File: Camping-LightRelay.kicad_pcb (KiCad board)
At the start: 2 copper layers, 43 x 63 mm, 62 parts, among them CN1 U262-061N-4BVC11, CN3 B2B-XH-A, CN4 907-152A1022D10200, CN5 907-152A1022D10200, J1 J300, J2 J300, J3 J300, J4 J300, Q1 IRF7404, Q2 BC847, U1 LMV358ID

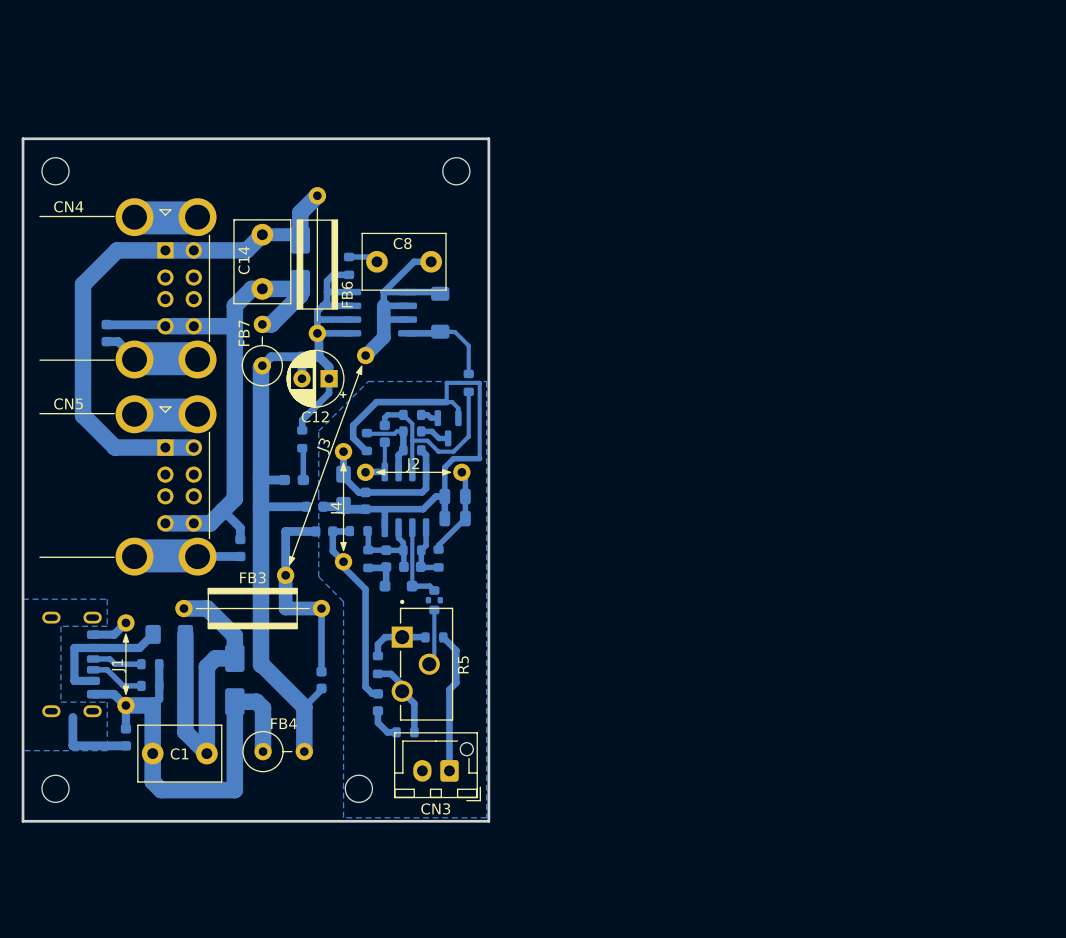
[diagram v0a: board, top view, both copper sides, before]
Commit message: Работа со схемой модуля
Частичная отрисовка и назначение посадочных мест субмодуля питания от PowerBank. *Работа продолжается*.
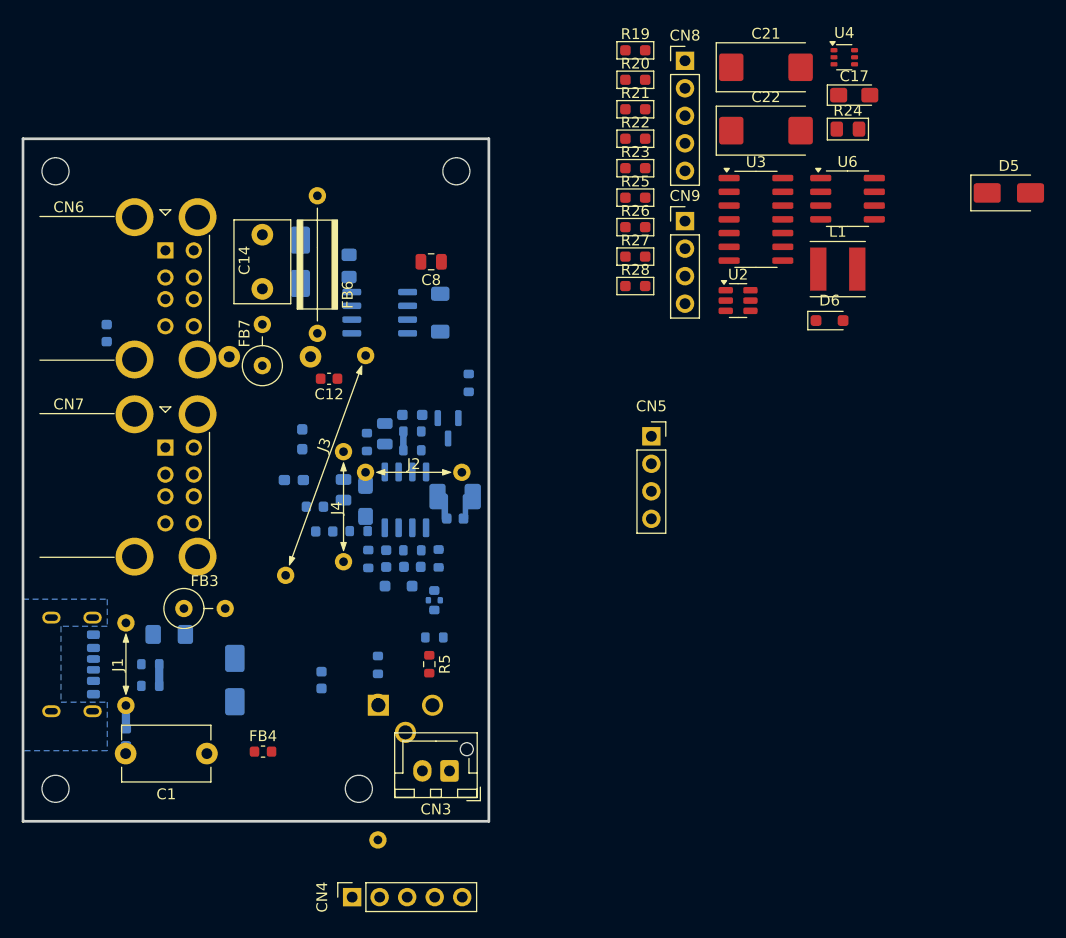
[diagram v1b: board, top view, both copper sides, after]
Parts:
- removed FB10: BLM18AG601SN1D, Inductor_SMD:L_0603_1608Metric
- added C17: 10uFx10V, Capacitor_Tantalum_SMD:CP_EIA-3216-12_Kemet-S_Pad1.58x1.35mm_HandSolder, F.Cu at (155.7, 39.0)
- added C21: 680uFx6.3V, Capacitor_Tantalum_SMD:CP_EIA-7343-43_Kemet-X_Pad2.25x2.55mm_HandSolder, F.Cu at (147.6, 36.4)
- added C22: 680uFx6.3V, Capacitor_Tantalum_SMD:CP_EIA-7343-43_Kemet-X_Pad2.25x2.55mm_HandSolder, F.Cu at (147.6, 42.2)
- added CN4: PM2.54-1*5, Connector_PinSocket_2.54mm:PinSocket_1x05_P2.54mm_Vertical, F.Cu at (109.4, 113.0)
- added CN5: PM2.54-1*4, Connector_PinSocket_2.54mm:PinSocket_1x04_P2.54mm_Vertical, F.Cu at (137.0, 70.5)
- added CN8: HB-PH3-25415PB2GOP, Connector_PinHeader_2.54mm:PinHeader_1x05_P2.54mm_Vertical, F.Cu at (140.1, 35.8)
- added CN9: HB-PH3-25414PB2GOP, Connector_PinHeader_2.54mm:PinHeader_1x04_P2.54mm_Vertical, F.Cu at (140.1, 50.6)
- added D5: SMAJ6.0A, Diode_SMD:D_SMA, F.Cu at (170.0, 48.0)
- added D6: SD05, Diode_SMD:D_SOD-323_HandSoldering, F.Cu at (153.4, 59.8)
- added L1: 47uH, Inductor_SMD:L_Taiyo-Yuden_NR-50xx, F.Cu at (154.2, 55.0)
- added R19: 2.7k, PCM_Resistor_SMD_AKL:R_0603_1608Metric_Pad0.98x0.95mm, F.Cu at (135.5, 34.8)
- added R20: 560, PCM_Resistor_SMD_AKL:R_0603_1608Metric_Pad0.98x0.95mm, F.Cu at (135.5, 37.6)
- added R21: 2.7k, PCM_Resistor_SMD_AKL:R_0603_1608Metric_Pad0.98x0.95mm, F.Cu at (135.5, 40.3)
- added R22: 10k, PCM_Resistor_SMD_AKL:R_0603_1608Metric_Pad0.98x0.95mm, F.Cu at (135.5, 43.0)
- added R23: 100k, PCM_Resistor_SMD_AKL:R_0603_1608Metric_Pad0.98x0.95mm, F.Cu at (135.5, 45.7)
- added R24: 10, PCM_Resistor_SMD_AKL:R_0805_2012Metric_Pad1.15x1.40mm, F.Cu at (155.1, 42.1)
- added R25: 2.7k, PCM_Resistor_SMD_AKL:R_0603_1608Metric_Pad0.98x0.95mm, F.Cu at (135.5, 48.4)
- added R26: 680k, PCM_Resistor_SMD_AKL:R_0603_1608Metric_Pad0.98x0.95mm, F.Cu at (135.5, 51.2)
- added R27: 22, PCM_Resistor_SMD_AKL:R_0603_1608Metric_Pad0.98x0.95mm, F.Cu at (135.5, 53.9)
- added R28: 1.2M, PCM_Resistor_SMD_AKL:R_0603_1608Metric_Pad0.98x0.95mm, F.Cu at (135.5, 56.6)
- added U2: USBLC6-2SC6, Package_TO_SOT_SMD:SOT-23-6, F.Cu at (145.0, 57.9)
- added U3: CD4011UBM, Package_SO:SOIC-14_3.9x8.7mm_P1.27mm, F.Cu at (146.7, 50.4)
- added U4: SI1865DDL, Package_TO_SOT_SMD:SOT-363_SC-70-6, F.Cu at (154.8, 35.5)
- added U6: TLC555DTR, Package_SO:SOIC-8_3.9x4.9mm_P1.27mm, F.Cu at (155.1, 48.5)
- C1: value 1500x2kV -> 2n2; footprint Capacitor_THT:C_Disc_D7.5mm_W5.0mm_P5.00mm -> Capacitor_THT:C_Disc_D8.0mm_W5.0mm_P7.50mm
- C10: value 10uF -> 56; footprint Capacitor_SMD:C_0805_2012Metric -> Capacitor_SMD:C_0603_1608Metric
- C11: value 0.1 -> 2n2; footprint Capacitor_SMD:C_0603_1608Metric -> Capacitor_THT:C_Disc_D8.0mm_W5.0mm_P7.50mm
- C12: value 100uFx10V -> 0.1; footprint Capacitor_THT:CP_Radial_D5.0mm_P2.50mm -> Capacitor_SMD:C_0603_1608Metric
- C13: value 56 -> 1uF; footprint Capacitor_SMD:C_0603_1608Metric -> Capacitor_SMD:C_0805_2012Metric
- C6: value 0.1 -> 10uFx10V; footprint Capacitor_SMD:C_0603_1608Metric -> Capacitor_Tantalum_SMD:CP_EIA-3216-10_Kemet-I_Pad1.58x1.35mm_HandSolder
- C7: value 10uFx10V -> 10uF; footprint Capacitor_Tantalum_SMD:CP_EIA-3216-10_Kemet-I_Pad1.58x1.35mm_HandSolder -> Capacitor_SMD:C_0805_2012Metric
- C8: value 1500x2kV -> 10uF; footprint Capacitor_THT:C_Disc_D7.5mm_W5.0mm_P5.00mm -> Capacitor_SMD:C_0805_2012Metric
- C9: value 10uF -> 100uFx10V; footprint Capacitor_SMD:C_0805_2012Metric -> Capacitor_Tantalum_SMD:CP_EIA-3528-15_AVX-H_Pad1.50x2.35mm_HandSolder
- D4: value SMAJ8.0A -> SMAJ6.0A
- FB2: value BLM18AG601SN1D -> XRRH3.5*8.0*0.8; footprint Inductor_SMD:L_0603_1608Metric -> PCM_Ferrite_THT_AKL:Ferrite_L8.0mm_D3.5mm_P12.70mm
- FB3: footprint PCM_Ferrite_THT_AKL:Ferrite_L8.0mm_D3.5mm_P12.70mm -> PCM_Ferrite_THT_AKL:Ferrite_L8.0mm_D3.5mm_P3.81mm_Vertical
- FB4: value XRRH3.5*8.0*0.8 -> BLM18AG601SN1D; footprint PCM_Ferrite_THT_AKL:Ferrite_L8.0mm_D3.5mm_P3.81mm_Vertical -> Inductor_SMD:L_0603_1608Metric
- R10: value 1.2M -> 2.2k
- R11: value 100k -> 120k
- R12: value 2.2k -> 560k
- R13: value 120k -> 10k
- R14: value 560k -> 10k
- R16, R17: value 10k -> 5.1k 1%; footprint Resistor_SMD:R_0603_1608Metric -> PCM_Resistor_SMD_AKL:R_0603_1608Metric_Pad0.98x0.95mm
- R18: value 1 -> 42; footprint Resistor_SMD:R_0603_1608Metric -> PCM_Resistor_SMD_AKL:R_0805_2012Metric_Pad1.15x1.40mm
- R3: value 5.1k 1% -> 180k 1%
- R4: value 180k 1% -> 200k; footprint Resistor_SMD:R_0603_1608Metric -> lib:TRIM_PTN10-A01HB20
- R5: value 200k -> 10k 1%; footprint lib:TRIM_PTN10-A01HB20 -> Resistor_SMD:R_0603_1608Metric
- R6: value 10k 1% -> 82k 1%
- R7: value 5.1k 1% -> 100k 1%
- R8: value 82k 1% -> 1.2M
- R9: value 100k 1% -> 100k
- renumbered CN4 to CN6, CN5 to CN7
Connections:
- C10 pad 1: Net-(J2-A) -> Net-(U1.2-+)
- C10 pad 2: GND -> Net-(CN5-Pin_3)
- C11 pad 1: Net-(C11-Pad1) -> Net-(CN6-VBUS1)
- C11 pad 2: GNDE -> Net-(CN6-GND1)
- C12 pad 1: Net-(C11-Pad1) -> /ScapPwrStorageModule/PBANK_VBUS
- C12 pad 2: GNDE -> GND2
- C13 pad 1: Net-(J2-B) -> Net-(D7-K)
- C13 pad 2: Net-(C13-Pad2) -> GND2
- C2 pad 1: Net-(R5-S) -> Net-(R4-S)
- C5 pad 1: +5V -> Net-(U1.1-V+)
- C5 pad 2: GNDE -> GND
- C6 pad 1: Net-(J4-A) -> Net-(U1.1-V+)
- C7 pad 1: Net-(J4-A) -> Net-(U1.2-+)
- C8 pad 1: Net-(D3-K) -> Net-(U1.2-+)
- C8 pad 2: Net-(C8-Pad2) -> GND
- C9 pad 1: Net-(J2-A) -> Net-(D4-A2)
- C9 pad 2: GND -> GNDE
- CN1 pad A12: Net-(J1-B) -> Net-(D1-A2)
- CN6 pad 1: Net-(CN4-VBUS1) -> Net-(CN6-VBUS1)
- CN6 pad 4: Net-(CN4-GND1) -> Net-(CN6-GND1)
- CN6 pad 5: Net-(CN4-VBUS1) -> Net-(CN6-VBUS1)
- CN6 pad 8: Net-(CN4-GND1) -> Net-(CN6-GND1)
- CN6 pad 9: Net-(CN4-Shield) -> Net-(CN6-Shield)
- CN7 pad 1: Net-(CN4-VBUS1) -> Net-(CN6-VBUS1)
- CN7 pad 4: Net-(CN4-GND1) -> Net-(CN6-GND1)
- CN7 pad 5: Net-(CN4-VBUS1) -> Net-(CN6-VBUS1)
- CN7 pad 8: Net-(CN4-GND1) -> Net-(CN6-GND1)
- CN7 pad 9: Net-(CN5-Shield) -> Net-(CN7-Shield)
- D3 pad 1: Net-(D3-K) -> Net-(CN4-Pin_1)
- D4 pad 1: Net-(CN4-VBUS1) -> Net-(CN4-Pin_1)
- D4 pad 2: Net-(CN4-GND1) -> Net-(D4-A2)
- FB2 pad 1: Net-(J4-B) -> Net-(D1-A1)
- FB2 pad 2: Net-(FB2-Pad2) -> Net-(CN4-Pin_1)
- FB3 pad 1: Net-(D1-A1) -> Net-(D1-A2)
- FB3 pad 2: +5V -> GNDE
- FB4 pad 1: Net-(D1-A2) -> Net-(CN5-Pin_4)
- FB4 pad 2: GNDE -> GND
- FB5 pad 2: Net-(J4-B) -> Net-(U1.1-V+)
- FB6 pad 1: Net-(C11-Pad1) -> Net-(D4-A2)
- FB6 pad 2: Net-(CN4-VBUS1) -> Net-(CN6-VBUS1)
- FB7 pad 2: Net-(CN4-GND1) -> Net-(CN6-GND1)
- FB8 pad 1: GNDE -> Net-(CN6-GND1)
- FB8 pad 2: GND -> Net-(CN6-Shield)
- FB9 pad 1: Net-(CN4-GND1) -> Net-(CN6-GND1)
- FB9 pad 2: Net-(CN4-Shield) -> Net-(CN7-Shield)
- Q1 pad 1: Net-(D3-K) -> Net-(CN4-Pin_1)
- Q1 pad 2: Net-(D3-K) -> Net-(CN4-Pin_1)
- Q1 pad 3: Net-(D3-K) -> Net-(CN4-Pin_1)
- Q1 pad 5: Net-(C11-Pad1) -> Net-(D4-A2)
- Q1 pad 6: Net-(C11-Pad1) -> Net-(D4-A2)
- Q1 pad 7: Net-(C11-Pad1) -> Net-(D4-A2)
- Q1 pad 8: Net-(C11-Pad1) -> Net-(D4-A2)
- R10 pad 1: Net-(U1.1-+) -> Net-(D3-A)
- R10 pad 2: Net-(C4-Pad2) -> Net-(CN5-Pin_3)
- R11 pad 1: Net-(C4-Pad2) -> Net-(U1.1-V+)
- R11 pad 2: Net-(J2-A) -> Net-(U1.2--)
- R12 pad 1: Net-(D3-A) -> Net-(U1.2--)
- R12 pad 2: Net-(C13-Pad2) -> GND
- R13 pad 1: Net-(J4-A) -> Net-(U1.2--)
- R13 pad 2: Net-(U1.2--) -> Net-(Q2-C)
- R14 pad 1: Net-(U1.2--) -> Net-(Q2-B)
- R14 pad 2: GND -> Net-(CN5-Pin_3)
- R15 pad 1: Net-(U1.2--) -> Net-(D4-A2)
- R15 pad 2: Net-(Q2-C) -> Net-(LED1-A)
- R16 pad 1: Net-(C11-Pad1) -> Net-(R16-Pad1)
- R16 pad 2: Net-(LED1-A) -> Net-(D6-A1)
- R17 pad 1: Net-(Q2-B) -> Net-(R17-Pad1)
- R17 pad 2: Net-(C13-Pad2) -> Net-(D6-A1)
- R18 pad 1: Net-(C8-Pad2) -> /ScapPwrStorageModule/PBANK_VBUS
- R18 pad 2: Net-(C11-Pad1) -> Net-(Q4-C)
- R2 pad 1: Net-(R5-E) -> Net-(R4-E)
- R2 pad 2: Net-(R5-A) -> Net-(R4-A)
- R3 pad 1: Net-(CN1-CC2) -> Net-(U1.1-V+)
- R3 pad 2: Net-(D1-A2) -> Net-(R4-E)
- R4 pad 1: Net-(FB2-Pad2) -> Net-(R4-A)
- R4 pad 2: Net-(R5-E) -> Net-(R4-S)
- R5 pad 1: Net-(R5-A) -> Net-(R4-A)
- R5 pad 2: Net-(R5-S) -> Net-(CN3-Pin_1)
- R6 pad 1: Net-(R5-A) -> Net-(U1.1-V+)
- R6 pad 2: Net-(CN3-Pin_1) -> Net-(U1.1-+)
- R7 pad 1: Net-(CN1-CC1) -> Net-(U1.1-+)
- R7 pad 2: Net-(D1-A2) -> GND
- R8 pad 1: Net-(J4-B) -> Net-(U1.1-+)
- R8 pad 2: Net-(U1.1-+) -> Net-(C4-Pad2)
- R9 pad 1: Net-(U1.1-+) -> Net-(C4-Pad2)
- R9 pad 2: GND -> Net-(U1.2-+)
- U1 pad 5: Net-(J2-B) -> Net-(U1.2-+)
- U1 pad 7: Net-(C13-Pad2) -> Net-(CN5-Pin_3)
- U1 pad 8: Net-(J4-A) -> Net-(U1.1-V+)
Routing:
- net Net-(CN4-GND1): track 53.1 -> 0.00 mm
- net GNDE: track 52.1 -> 0.00 mm
- net Net-(CN4-VBUS1): track 50.4 -> 0.00 mm
- net GND: track 51.9 -> 4.03 mm
- net Net-(D1-A2): track 42.1 -> 2.15 mm
- net Net-(D1-A1): track 30.5 -> 0.00 mm
- net Net-(C11-Pad1): track 29.2 -> 0.00 mm
- net Net-(D3-K): track 21.7 -> 0.00 mm
- net +5V: track 19.0 -> 0.00 mm
- net Net-(J4-B): track 18.6 -> 0.00 mm
- net Net-(C13-Pad2): track 18.5 -> 0.00 mm
- net Net-(CN5-Shield): track 15.5 -> 0.00 mm
- net Net-(CN4-Shield): track 15.4 -> 0.00 mm
- net Net-(J4-A): track 14.8 -> 0.00 mm
- net Net-(CN3-Pin_1): track 13.1 -> 0.00 mm
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- removed copper zone on B.Cu, net GND

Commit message: Переделка топологии субмодулей
Фотореле вынесен в отдельный субмодуль, как дополнительная печатная плата. Схема управления PowerBank-ом перенесена на силовую плату с другими компонентами.
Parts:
- moved CN8 27.9 mm to (127.0, 60.4)
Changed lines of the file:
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@@
 	(footprint "Connector_PinHeader_2.54mm:PinHeader_1x05_P2.54mm_Vertical"
 		(layer "F.Cu")
-		(at 140.105 35.8)
+		(at 127 60.38)
 		(descr "Through hole straight pin header, 1x05, 2.54mm pitch, single row")
 		(tags "Through hole pin header THT 1x05 2.54mm single row")
@@
 		)
 		(fp_text user "${REFERENCE}"
-			(at 0 5.08 360)
+			(at 0 5.08 0)
 			(layer "F.Fab")
 			(effects

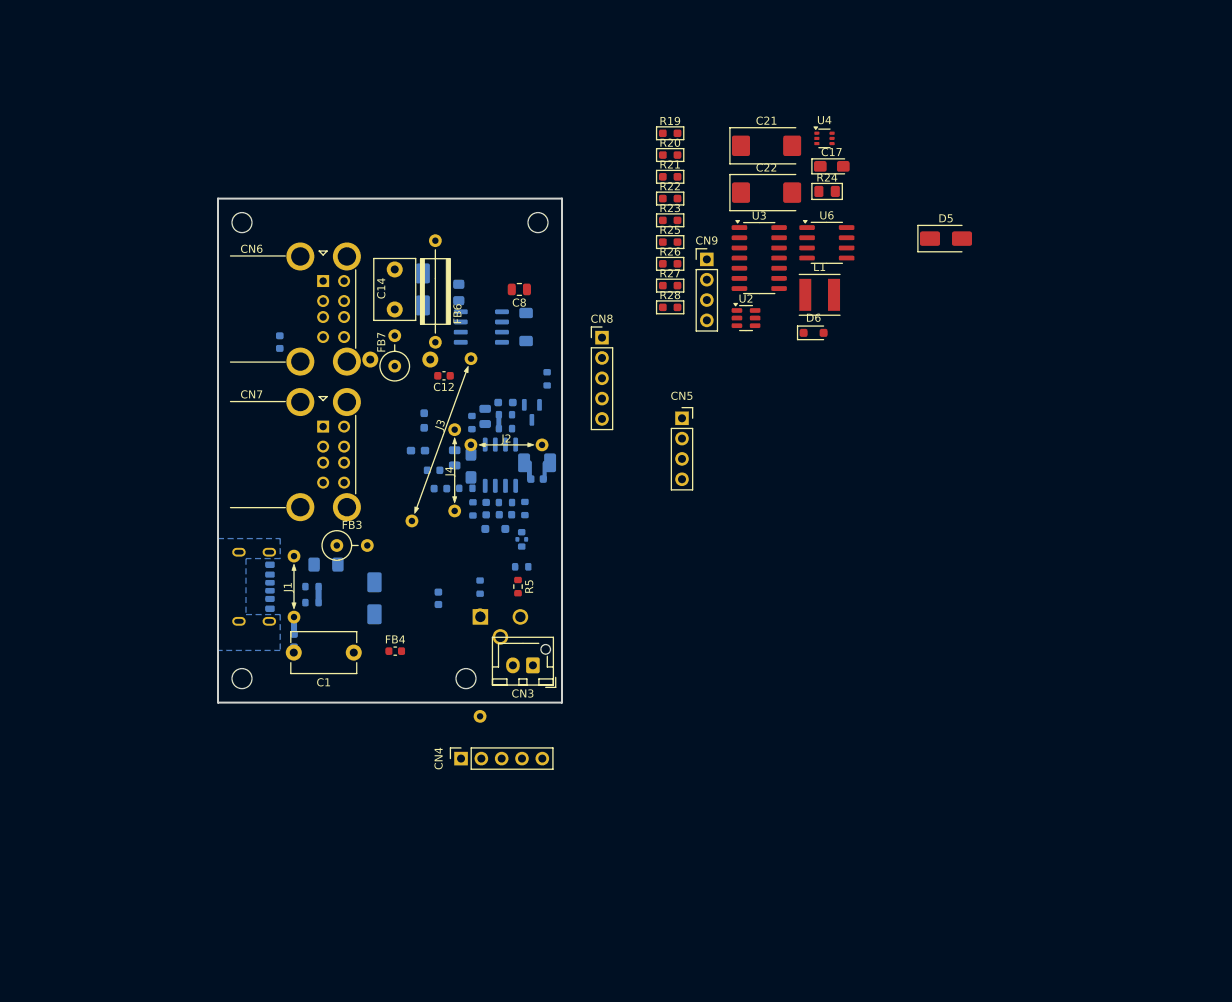
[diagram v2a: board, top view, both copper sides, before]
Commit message: Назначение посадочных мест схемы
Дорисовка недостающий э/компонентов и важных 3D-моделей
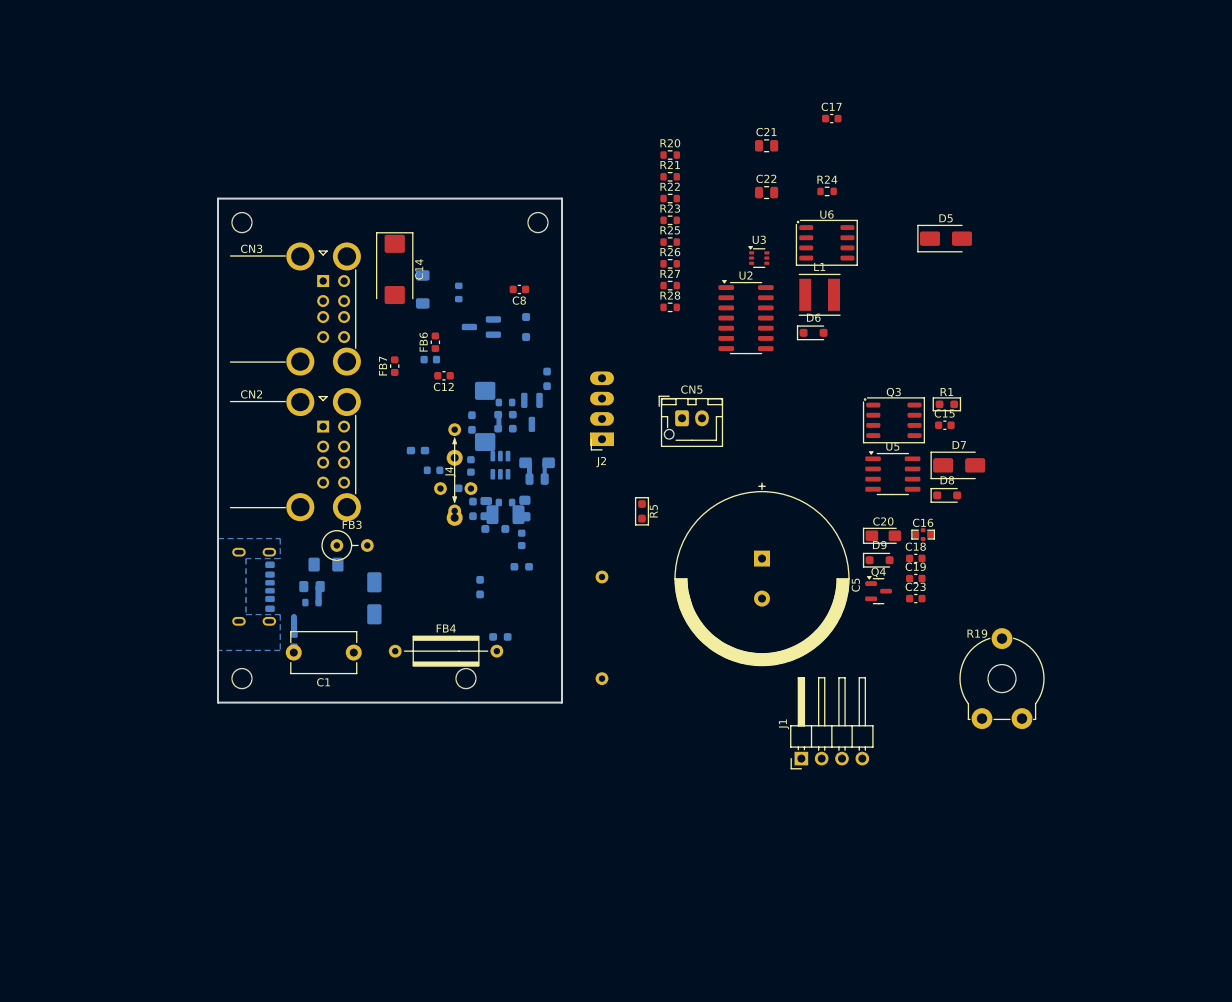
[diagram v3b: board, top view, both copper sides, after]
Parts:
- removed the CN3 at (118.4, 101.3)
- removed CN4: PM2.54-1*5, Connector_PinSocket_2.54mm:PinSocket_1x05_P2.54mm_Vertical
- removed CN8: HB-PH3-25415PB2GOP, Connector_PinHeader_2.54mm:PinHeader_1x05_P2.54mm_Vertical
- removed CN9: HB-PH3-25414PB2GOP, Connector_PinHeader_2.54mm:PinHeader_1x04_P2.54mm_Vertical
- removed FB9: BLM18AG601SN1D, Inductor_SMD:L_0603_1608Metric
- removed J3: J300, lib:Junction_850mil
- removed R16: 5.1k 1%, PCM_Resistor_SMD_AKL:R_0603_1608Metric_Pad0.98x0.95mm
- removed U4: SI1865DDL, Package_TO_SOT_SMD:SOT-363_SC-70-6
- added C15: 0.1, Capacitor_SMD:C_0603_1608Metric, F.Cu at (169.9, 71.3)
- added C16: 0.1, lib:C_0603_3-terminal, F.Cu at (167.1, 85.0)
- added C18: 56, Capacitor_SMD:C_0603_1608Metric, F.Cu at (166.2, 88.0)
- added C19: 0.1, Capacitor_SMD:C_0603_1608Metric, F.Cu at (166.2, 90.5)
- added C20: 10uFx10V, Capacitor_Tantalum_SMD:CP_EIA-3216-10_Kemet-I_Pad1.58x1.35mm_HandSolder, F.Cu at (162.2, 85.2)
- added C23: 56, Capacitor_SMD:C_0603_1608Metric, F.Cu at (166.2, 93.0)
- added D7: SMAJ6.0A, Diode_SMD:D_SMA, F.Cu at (171.7, 76.3)
- added D8: BAT20J, Diode_SMD:D_SOD-323_HandSoldering, F.Cu at (170.2, 80.1)
- added D9: SD05, Diode_SMD:D_SOD-323_HandSoldering, F.Cu at (161.7, 88.2)
- added Q3: IRF7404, PCM_Package_SO_AKL:SO-8_3.9x4.9mm_P1.27mm, F.Cu at (163.5, 70.7)
- added Q4: BC847, Package_TO_SOT_SMD:SOT-23, F.Cu at (161.6, 92.1)
- added R1: 5.1k 1%, PCM_Resistor_SMD_AKL:R_0603_1608Metric_Pad0.98x0.95mm, F.Cu at (170.1, 68.7)
- added U5: TLC555DTR, Package_SO:SOIC-8_3.9x4.9mm_P1.27mm, F.Cu at (163.4, 77.4)
- C10: value 56 -> 1uF; footprint Capacitor_SMD:C_0603_1608Metric -> Capacitor_SMD:C_0805_2012Metric
- C11: value 2n2 -> 0.1; footprint Capacitor_THT:C_Disc_D8.0mm_W5.0mm_P7.50mm -> Capacitor_SMD:C_0603_1608Metric
- C13: value 1uF -> 680uFx6.3V; footprint Capacitor_SMD:C_0805_2012Metric -> Capacitor_Tantalum_SMD:CP_EIA-7343-43_Kemet-X_Pad2.25x2.55mm_HandSolder
- C14: value 1500x2kV -> 680uFx6.3V; footprint Capacitor_THT:C_Disc_D7.5mm_W5.0mm_P5.00mm -> Capacitor_Tantalum_SMD:CP_EIA-7343-43_Kemet-X_Pad2.25x2.55mm_HandSolder
- C17: value 10uFx10V -> 0.1; footprint Capacitor_Tantalum_SMD:CP_EIA-3216-12_Kemet-S_Pad1.58x1.35mm_HandSolder -> Capacitor_SMD:C_0603_1608Metric
- C2: footprint lib:C_0603_3-terminal -> Capacitor_SMD:C_0603_1608Metric
- C21, C22: value 680uFx6.3V -> 10uF; footprint Capacitor_Tantalum_SMD:CP_EIA-7343-43_Kemet-X_Pad2.25x2.55mm_HandSolder -> Capacitor_SMD:C_0805_2012Metric
- C3: value 0.1 -> 1uF; footprint Capacitor_SMD:C_0603_1608Metric -> Capacitor_SMD:C_0805_2012Metric
- C4: value 56 -> 100uFx10V; footprint Capacitor_SMD:C_0603_1608Metric -> Capacitor_Tantalum_SMD:CP_EIA-3528-15_AVX-H_Pad1.50x2.35mm_HandSolder
- C5: value 0.1 -> 1.5Fx5.5V; footprint Capacitor_SMD:C_0603_1608Metric -> lib:Eaton_KR-5R5C155; moved to F.Cu
- C6: value 10uFx10V -> 10n; footprint Capacitor_Tantalum_SMD:CP_EIA-3216-10_Kemet-I_Pad1.58x1.35mm_HandSolder -> Capacitor_SMD:C_0603_1608Metric
- C7: value 10uF -> 2n2; footprint Capacitor_SMD:C_0805_2012Metric -> Capacitor_THT:C_Disc_D8.0mm_W5.0mm_P7.50mm
- C8: value 10uF -> 10n; footprint Capacitor_SMD:C_0805_2012Metric -> Capacitor_SMD:C_0603_1608Metric
- C9: value 100uFx10V -> 10uFx10V; footprint Capacitor_Tantalum_SMD:CP_EIA-3528-15_AVX-H_Pad1.50x2.35mm_HandSolder -> Capacitor_Tantalum_SMD:CP_EIA-3216-12_Kemet-S_Pad1.58x1.35mm_HandSolder
- CN5: value PM2.54-1*4 -> B2B-XH-A; footprint Connector_PinSocket_2.54mm:PinSocket_1x04_P2.54mm_Vertical -> Connector_JST:JST_XH_B2B-XH-AM_1x02_P2.50mm_Vertical
- D3: value BZV55C6V8 -> BAT20J; footprint Diode_SMD:D_MiniMELF -> Diode_SMD:D_SOD-323_HandSoldering
- D4: value SMAJ6.0A -> BZV55C6V8; footprint Diode_SMD:D_SMA -> Diode_SMD:D_MiniMELF
- D6: value SD05 -> BAT20J
- FB4: value BLM18AG601SN1D -> XRRH3.5*8.0*0.8; footprint Inductor_SMD:L_0603_1608Metric -> PCM_Ferrite_THT_AKL:Ferrite_L8.0mm_D3.5mm_P12.70mm
- FB5: value BLM18AG601SN1D -> XRRH3.5*8.0*0.8; footprint Inductor_SMD:L_0603_1608Metric -> PCM_Ferrite_THT_AKL:Ferrite_L8.0mm_D3.5mm_P3.81mm_Vertical
- FB6: value XRRH3.5*8.0*0.8 -> BLM18AG601SN1D; footprint PCM_Ferrite_THT_AKL:Ferrite_L8.0mm_D3.5mm_P12.70mm -> Inductor_SMD:L_0603_1608Metric
- FB7: value XRRH3.5*8.0*0.8 -> BLM18AG601SN1D; footprint PCM_Ferrite_THT_AKL:Ferrite_L8.0mm_D3.5mm_P3.81mm_Vertical -> Inductor_SMD:L_0603_1608Metric
- J1: value J300 -> PH2.54-07-04PWD; footprint lib:Junction_300mil -> Connector_PinHeader_2.54mm:PinHeader_1x04_P2.54mm_Horizontal
- J2: value J300 -> ~; footprint lib:Junction_350mil -> lib:PinSolder_1x04_P2.54mm
- Q1: value IRF7404 -> FDV301N; footprint PCM_Package_SO_AKL:SO-8_3.9x4.9mm_P1.27mm -> PCM_Package_TO_SOT_SMD_AKL:SOT-23_BigPads
- Q2: value BC847 -> BC817; footprint Package_TO_SOT_SMD:SOT-23 -> PCM_Package_TO_SOT_SMD_AKL:SOT-23_BigPads
- R10: value 2.2k -> 10k
- R11: value 120k -> 10; footprint Resistor_SMD:R_0603_1608Metric -> PCM_Resistor_SMD_AKL:R_0805_2012Metric_Pad1.15x1.40mm
- R12: value 560k -> 2.7k; footprint Resistor_SMD:R_0603_1608Metric -> PCM_Resistor_SMD_AKL:R_0603_1608Metric_Pad0.98x0.95mm
- R13: value 10k -> 680k; footprint Resistor_SMD:R_0603_1608Metric -> PCM_Resistor_SMD_AKL:R_0603_1608Metric_Pad0.98x0.95mm
- R14: value 10k -> 22; footprint Resistor_SMD:R_0603_1608Metric -> PCM_Resistor_SMD_AKL:R_0603_1608Metric_Pad0.98x0.95mm
- R15: value 10k -> 1.2M; footprint Resistor_SMD:R_0603_1608Metric -> PCM_Resistor_SMD_AKL:R_0603_1608Metric_Pad0.98x0.95mm
- R17: value 5.1k 1% -> 1.8M; footprint PCM_Resistor_SMD_AKL:R_0603_1608Metric_Pad0.98x0.95mm -> Resistor_SMD:R_0603_1608Metric
- R18: value 42 -> 180k 1%; footprint PCM_Resistor_SMD_AKL:R_0805_2012Metric_Pad1.15x1.40mm -> Resistor_SMD:R_0603_1608Metric
- R19: value 2.7k -> 200k; footprint PCM_Resistor_SMD_AKL:R_0603_1608Metric_Pad0.98x0.95mm -> lib:Potentiometer_Bochen_PT10
- R2: value 1.8M -> 5.1k 1%; footprint Resistor_SMD:R_0603_1608Metric -> PCM_Resistor_SMD_AKL:R_0603_1608Metric_Pad0.98x0.95mm
- R20: value 560 -> 10k 1%; footprint PCM_Resistor_SMD_AKL:R_0603_1608Metric_Pad0.98x0.95mm -> Resistor_SMD:R_0603_1608Metric
- R21: value 2.7k -> 82k 1%; footprint PCM_Resistor_SMD_AKL:R_0603_1608Metric_Pad0.98x0.95mm -> Resistor_SMD:R_0603_1608Metric
- R22: value 10k -> 100k 1%; footprint PCM_Resistor_SMD_AKL:R_0603_1608Metric_Pad0.98x0.95mm -> Resistor_SMD:R_0603_1608Metric
- R23: value 100k -> 1.2M; footprint PCM_Resistor_SMD_AKL:R_0603_1608Metric_Pad0.98x0.95mm -> Resistor_SMD:R_0603_1608Metric
- R24: value 10 -> 100k; footprint PCM_Resistor_SMD_AKL:R_0805_2012Metric_Pad1.15x1.40mm -> Resistor_SMD:R_0603_1608Metric
- R25: value 2.7k -> 120k; footprint PCM_Resistor_SMD_AKL:R_0603_1608Metric_Pad0.98x0.95mm -> Resistor_SMD:R_0603_1608Metric
- R26: value 680k -> 560k; footprint PCM_Resistor_SMD_AKL:R_0603_1608Metric_Pad0.98x0.95mm -> Resistor_SMD:R_0603_1608Metric
- R27: value 22 -> 10k; footprint PCM_Resistor_SMD_AKL:R_0603_1608Metric_Pad0.98x0.95mm -> Resistor_SMD:R_0603_1608Metric
- R28: value 1.2M -> 10k; footprint PCM_Resistor_SMD_AKL:R_0603_1608Metric_Pad0.98x0.95mm -> Resistor_SMD:R_0603_1608Metric
- R3: value 180k 1% -> 42; footprint Resistor_SMD:R_0603_1608Metric -> PCM_Resistor_SMD_AKL:R_0805_2012Metric_Pad1.15x1.40mm
- R4: value 200k -> 2.7k; footprint lib:TRIM_PTN10-A01HB20 -> PCM_Resistor_SMD_AKL:R_0603_1608Metric_Pad0.98x0.95mm
- R5: value 10k 1% -> 560; footprint Resistor_SMD:R_0603_1608Metric -> PCM_Resistor_SMD_AKL:R_0603_1608Metric_Pad0.98x0.95mm
- R6: value 82k 1% -> 2.7k; footprint Resistor_SMD:R_0603_1608Metric -> PCM_Resistor_SMD_AKL:R_0603_1608Metric_Pad0.98x0.95mm
- R7: value 100k 1% -> 2.2k
- R8: value 1.2M -> 10k; footprint Resistor_SMD:R_0603_1608Metric -> PCM_Resistor_SMD_AKL:R_0603_1608Metric_Pad0.98x0.95mm
- R9: footprint Resistor_SMD:R_0603_1608Metric -> PCM_Resistor_SMD_AKL:R_0603_1608Metric_Pad0.98x0.95mm
- U1: value LMV358ID -> USBLC6-2SC6; footprint PCM_Package_SO_AKL:SO-8_3.9x4.9mm_P1.27mm -> Package_TO_SOT_SMD:SOT-23-6
- U2: value USBLC6-2SC6 -> CD4011UBM; footprint Package_TO_SOT_SMD:SOT-23-6 -> Package_SO:SOIC-14_3.9x8.7mm_P1.27mm
- U3: value CD4011UBM -> SI1865DDL; footprint Package_SO:SOIC-14_3.9x8.7mm_P1.27mm -> Package_TO_SOT_SMD:SOT-363_SC-70-6
- U6: value TLC555DTR -> LMV358ID; footprint Package_SO:SOIC-8_3.9x4.9mm_P1.27mm -> PCM_Package_SO_AKL:SO-8_3.9x4.9mm_P1.27mm
- moved R19 82.9 mm to (174.5, 108.0)
- moved J1 65.8 mm to (151.9, 113.0)
- moved C5 40.8 mm to (147.0, 88.0)
- moved R5 18.1 mm to (132.0, 82.1)
- moved FB2 16.0 mm to (127.0, 90.3)
- moved J2 7.53 mm to (127.0, 73.1)
- moved C17 5.97 mm to (155.7, 33.0)
- renumbered CN7 to CN2, CN6 to CN3
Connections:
- C10 pad 1: Net-(U1.2-+) -> GND2
- C10 pad 2: Net-(CN5-Pin_3) -> VCC
- C11 pad 1: Net-(CN6-VBUS1) -> GND2
- C11 pad 2: Net-(CN6-GND1) -> VCC
- C12 pad 1: /ScapPwrStorageModule/PBANK_VBUS -> GNDE
- C12 pad 2: GND2 -> VCC
- C13 pad 1: Net-(D7-K) -> Net-(U5-THR)
- C13 pad 2: GND2 -> GNDE
- C14 pad 1: Net-(CN4-VBUS1) -> Net-(U5-THR)
- C14 pad 2: Net-(CN4-GND1) -> GNDE
- C17 pad 1: VCC -> Net-(U6.1-+)
- C17 pad 2: GND2 -> GND
- C2 pad 1: Net-(R4-S) -> Net-(D3-A)
- C2 pad 2: GND -> GNDE
- C21 pad 1: Net-(U6-THR) -> Net-(U6.2-+)
- C21 pad 2: GND2 -> GND
- C22 pad 1: Net-(U6-THR) -> Net-(U6.2-+)
- C22 pad 2: GND2 -> GND
- C3 pad 1: Net-(U1.1-+) -> Net-(D3-K)
- C3 pad 2: GND -> GNDE
- C4 pad 1: Net-(U1.1-+) -> Net-(D5-A2)
- C4 pad 2: Net-(C4-Pad2) -> GNDE
- C5 pad 1: Net-(U1.1-V+) -> Net-(D6-A)
- C5 pad 2: GND -> GNDE
- C6 pad 1: Net-(U1.1-V+) -> Net-(U5-TR)
- C6 pad 2: GND -> GNDE
- C7 pad 1: Net-(U1.2-+) -> Net-(CN2-VBUS1)
- C7 pad 2: GND -> Net-(CN2-GND1)
- C8 pad 1: Net-(U1.2-+) -> Net-(U5-CV)
- C8 pad 2: GND -> GNDE
- C9 pad 1: Net-(D4-A2) -> VCC
- CN2 pad 1: Net-(CN6-VBUS1) -> Net-(CN2-VBUS1)
- CN2 pad 4: Net-(CN6-GND1) -> Net-(CN2-GND1)
- CN2 pad 5: Net-(CN6-VBUS1) -> Net-(CN2-VBUS1)
- CN2 pad 8: Net-(CN6-GND1) -> Net-(CN2-GND1)
- CN2 pad 9: Net-(CN7-Shield) -> Net-(CN2-Shield)
- CN3 pad 1: Net-(CN6-VBUS1) -> Net-(CN2-VBUS1)
- CN3 pad 4: Net-(CN6-GND1) -> Net-(CN2-GND1)
- CN3 pad 5: Net-(CN6-VBUS1) -> Net-(CN2-VBUS1)
- CN3 pad 8: Net-(CN6-GND1) -> Net-(CN2-GND1)
- CN3 pad 9: Net-(CN6-Shield) -> Net-(CN3-Shield)
- CN5 pad 1: +5V -> Net-(CN5-Pin_1)
- CN5 pad 2: unconnected-(CN5-Pin_2-Pad2) -> GND
- D2 pad 2: GND -> GNDE
- D3 pad 1: Net-(CN4-Pin_1) -> Net-(D3-K)
- D4 pad 1: Net-(CN4-Pin_1) -> Net-(D3-A)
- D4 pad 2: Net-(D4-A2) -> Net-(D4-A)
- D5 pad 1: Net-(CN6-VBUS1) -> Net-(D3-A)
- D5 pad 2: Net-(CN6-GND1) -> Net-(D5-A2)
- D6 pad 1: Net-(D6-A1) -> Net-(D3-K)
- D6 pad 2: GND2 -> Net-(D6-A)
- FB2 pad 2: Net-(CN4-Pin_1) -> Net-(D3-A)
- FB4 pad 1: Net-(CN5-Pin_4) -> Net-(D5-A2)
- FB4 pad 2: GND -> Net-(CN2-VBUS1)
- FB5 pad 1: +5V -> GNDE
- FB5 pad 2: Net-(U1.1-V+) -> Net-(CN2-GND1)
- FB6 pad 1: Net-(D4-A2) -> Net-(CN2-GND1)
- FB6 pad 2: Net-(CN6-VBUS1) -> Net-(CN2-Shield)
- FB7 pad 1: GNDE -> Net-(CN2-GND1)
- FB7 pad 2: Net-(CN6-GND1) -> Net-(CN3-Shield)
- FB8 pad 1: Net-(CN6-GND1) -> /Субмодуль фотореле/+5V
- FB8 pad 2: Net-(CN6-Shield) -> Net-(U6.1-V+)
- J1 pad 1: Net-(D1-A2) -> /Субмодуль фотореле/+5V
- J1 pad 2: Net-(J1-B) -> /Субмодуль фотореле/~{RELAY_ON}
- J2 pad 1: Net-(J2-A) -> VCC
- J2 pad 2: Net-(J2-B) -> /~{LOAD_ON}
- L1 pad 1: Net-(D7-K) -> Net-(D3-K)
- Q1 pad 1: Net-(CN4-Pin_1) -> Net-(Q1-G)
- Q1 pad 2: Net-(CN4-Pin_1) -> GNDE
- Q1 pad 3: Net-(CN4-Pin_1) -> Net-(D2-A1)
- Q2 pad 2: GND -> GNDE
- R10 pad 1: Net-(D3-A) -> Net-(D5-A2)
- R10 pad 2: Net-(CN5-Pin_3) -> Net-(LED1-A)
- R11 pad 1: Net-(U1.1-V+) -> Net-(D3-K)
- R11 pad 2: Net-(U1.2--) -> Net-(D6-A)
- R12 pad 1: Net-(U1.2--) -> Net-(D6-A)
- R12 pad 2: GND -> Net-(U5-TR)
- R13 pad 1: Net-(U1.2--) -> Net-(U5-CV)
- R13 pad 2: Net-(Q2-C) -> VCC
- R14 pad 1: Net-(Q2-B) -> Net-(U5-DIS)
- R14 pad 2: Net-(CN5-Pin_3) -> Net-(U5-THR)
- R15 pad 1: Net-(D4-A2) -> Net-(U5-THR)
- R15 pad 2: Net-(LED1-A) -> VCC
- R17 pad 1: Net-(R17-Pad1) -> Net-(R19-E)
- R17 pad 2: Net-(D6-A1) -> Net-(R19-A)
- R18 pad 1: /ScapPwrStorageModule/PBANK_VBUS -> Net-(U6.1-V+)
- R18 pad 2: Net-(Q4-C) -> Net-(R19-E)
- R19 pad 1: Net-(R19-Pad1) -> Net-(R19-A)
- R2 pad 1: Net-(R4-E) -> Net-(R2-Pad1)
- R2 pad 2: Net-(R4-A) -> Net-(D2-A1)
- R20 pad 1: Net-(R20-Pad1) -> Net-(R19-A)
- R20 pad 2: GND2 -> Net-(CN5-Pin_1)
- R21 pad 1: Net-(Q3-G) -> Net-(U6.1-V+)
- R21 pad 2: Net-(R21-Pad2) -> Net-(U6.1-+)
- R22 pad 1: Net-(R22-Pad1) -> Net-(U6.1-+)
- R22 pad 2: Net-(D7-K) -> GND
- R23 pad 1: /ScapPwrStorageModule/~{SWON_IN} -> Net-(U6.1-+)
- R23 pad 2: VCC -> Net-(C18-Pad2)
- R24 pad 1: Net-(D7-K) -> Net-(C18-Pad2)
- R24 pad 2: Net-(D8-A) (its old number) -> Net-(U6.2-+)
- R25 pad 1: Net-(D8-A) (its old number) -> Net-(U6.1-V+)
- R25 pad 2: Net-(U6-TR) -> Net-(U6.2--)
- R26 pad 1: Net-(U6-CV) -> Net-(U6.2--)
- R26 pad 2: VCC -> GND
- R27 pad 1: Net-(U6-DIS) -> Net-(U6.2--)
- R27 pad 2: Net-(U6-THR) -> Net-(Q4-C)
- R28 pad 1: Net-(U6-THR) -> Net-(Q4-B)
- R28 pad 2: VCC -> /Субмодуль фотореле/~{RELAY_ON}
- R3 pad 1: Net-(U1.1-V+) -> Net-(D3-A)
- R3 pad 2: Net-(R4-E) -> Net-(Q2-C)
- R4 pad 1: Net-(R4-A) -> Net-(R4-Pad1)
- R4 pad 2: Net-(R4-S) -> Net-(Q2-B)
- R5 pad 1: Net-(R4-A) -> Net-(R5-Pad1)
- R5 pad 2: Net-(CN3-Pin_1) -> GNDE
- R6 pad 1: Net-(U1.1-V+) -> Net-(Q1-G)
- R6 pad 2: Net-(U1.1-+) -> Net-(R6-Pad2)
- R7 pad 1: Net-(U1.1-+) -> Net-(D4-A)
- R7 pad 2: GND -> /~{LOAD_ON}
- R8 pad 1: Net-(U1.1-+) -> Net-(R8-Pad1)
- R8 pad 2: Net-(C4-Pad2) -> Net-(D3-K)
- R9 pad 1: Net-(C4-Pad2) -> /~{LOAD_ON}
- R9 pad 2: Net-(U1.2-+) -> VCC
- U1 pad 1: Net-(C4-Pad2) -> Net-(CN1-CC1)
- U1 pad 2: Net-(D2-A1) -> GNDE
- U1 pad 3: Net-(U1.1-+) -> Net-(CN1-CC2)
- U1 pad 4: GND -> Net-(R1-Pad1)
- U1 pad 5: Net-(U1.2-+) -> Net-(D3-A)
- U1 pad 6: Net-(U1.2--) -> Net-(R2-Pad1)
- U2 pad 1: /ScapPwrStorageModule/CC1 -> Net-(U2-Pad1)
- U2 pad 2: GNDPWR -> Net-(U2-Pad1)
- U2 pad 3: /ScapPwrStorageModule/CC2 -> Net-(R4-Pad1)
- U2 pad 4: Net-(R16-Pad1) -> Net-(U2-Pad1)
- U2 pad 5: /ScapPwrStorageModule/PBANK_VBUS -> Net-(R6-Pad2)
- U2 pad 6: Net-(R17-Pad1) -> /~{LOAD_ON}
- U3 pad 1: Net-(U3-Pad1) -> Net-(R5-Pad1)
- U3 pad 2: Net-(U3-Pad1) -> Net-(D3-A)
- U3 pad 3: Net-(R19-Pad1) -> Net-(D3-A)
- U3 pad 4: Net-(U3-Pad1) -> Net-(D3-K)
- U3 pad 5: Net-(R21-Pad2) -> Net-(Q1-G)
- U3 pad 6: /ScapPwrStorageModule/~{SWON_IN} -> Net-(R8-Pad1)
- U6 pad 1: GND2 -> Net-(C18-Pad2)
- U6 pad 2: Net-(U6-TR) -> Net-(D9-A1)
- U6 pad 3: Net-(U6-Q) -> Net-(U6.1-+)
- U6 pad 4: VCC -> GND
- U6 pad 5: Net-(U6-CV) -> Net-(U6.2-+)
- U6 pad 6: Net-(U6-THR) -> Net-(U6.2--)
- U6 pad 7: Net-(U6-DIS) -> /Субмодуль фотореле/~{RELAY_ON}
- U6 pad 8: VCC -> Net-(U6.1-V+)
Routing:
- net (no net): track 0.00 -> 4.03 mm
- net Net-(J2-A): track 2.03 -> 0.00 mm
- net GND: track 4.03 -> 2.03 mm
